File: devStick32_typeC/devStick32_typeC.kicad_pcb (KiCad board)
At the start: 2 copper layers, 35.6 x 82.6 mm, 9 parts, among them J1 Conn_01x06_Male, J2 Conn_01x14_Male, J3 Conn_01x14_Male, J4 Conn_02x05_Odd_Even, J5 CX70M-24P1

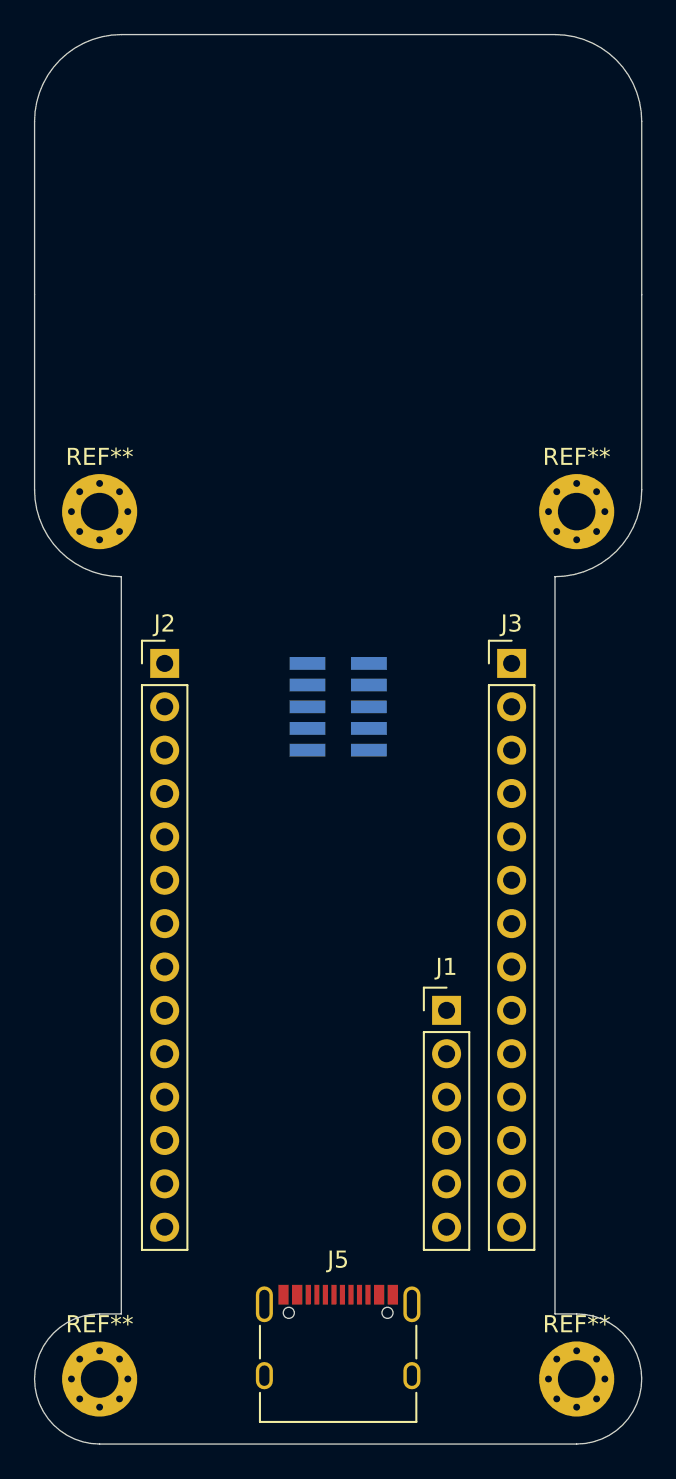
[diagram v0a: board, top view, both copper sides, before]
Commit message: Added ESP32-D0 on schema and PCB
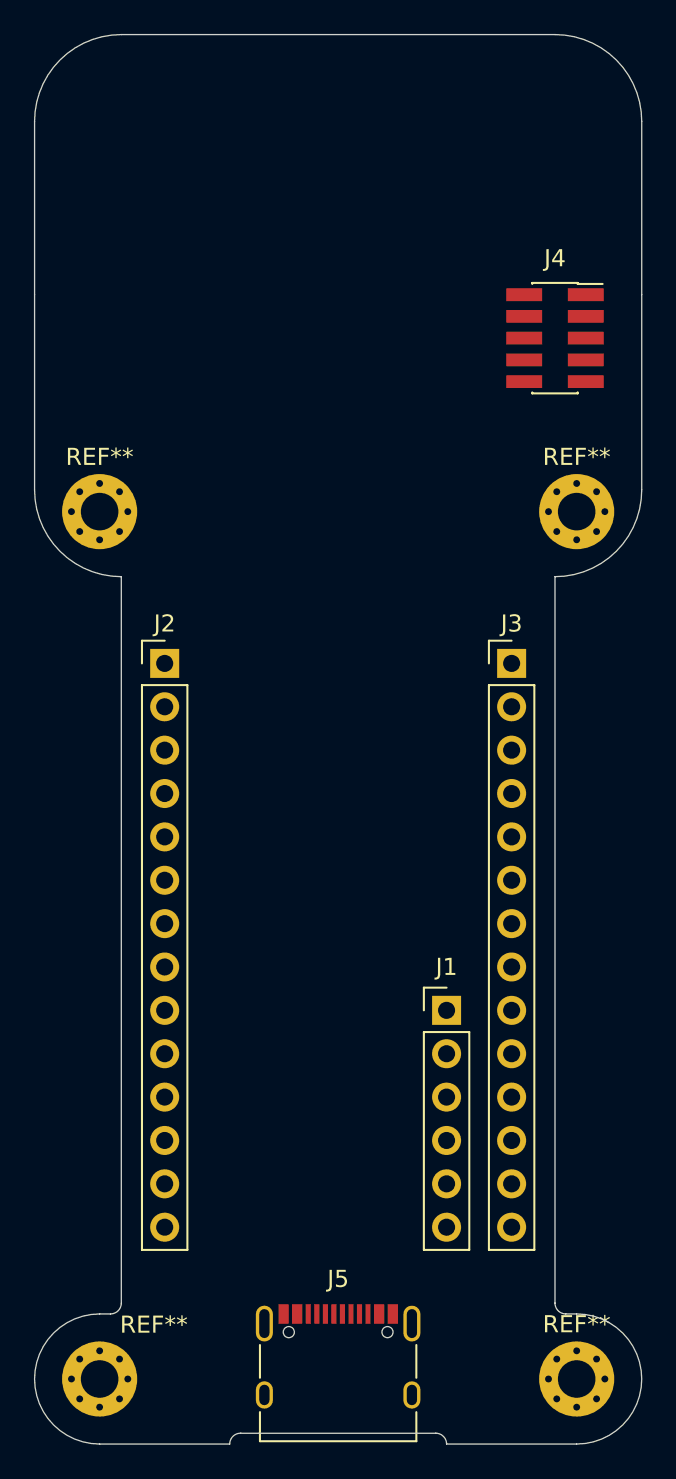
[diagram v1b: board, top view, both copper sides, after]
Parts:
- J4: moved to F.Cu
- moved J4 25.0 mm to (172.7, 64.8)
- moved J5 1.13 mm to (160.0, 125.6)
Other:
- outline, holes or cut-outs redrawn

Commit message: Added memory, xtal and labels
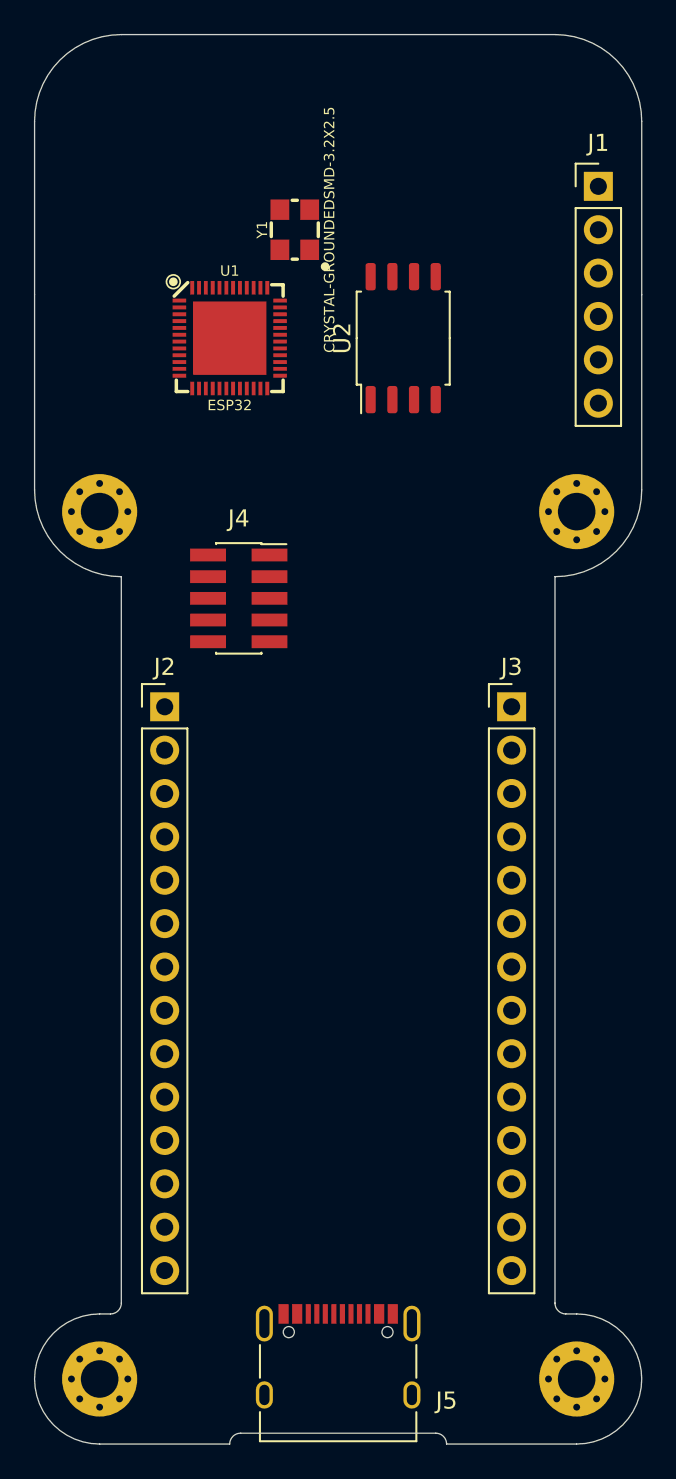
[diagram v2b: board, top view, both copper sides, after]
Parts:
- added U1: ESP32, Silicon-Standard:QFN48-0.4MM, F.Cu at (153.7, 64.8)
- added U2: W25Q32JVSS, Package_SO:SOIC-8_5.23x5.23mm_P1.27mm, F.Cu at (163.8, 64.8)
- added Y1: CRYSTAL-GROUNDEDSMD-3.2X2.5, CRYSTAL-SMD-3.2X2.5MM, F.Cu at (157.5, 58.4)
- moved J1 49.1 mm to (175.3, 55.9)
- moved J4 24.0 mm to (154.2, 80.0)
- moved J2 2.54 mm to (149.9, 86.4)
- moved J3 2.54 mm to (170.2, 86.4)
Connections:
- net Net-(J2-Pad10) renamed GPIO_8
- net Net-(J2-Pad11) renamed GPIO_9
- net Net-(J2-Pad12) renamed GPIO_10
- net Net-(J2-Pad13) renamed USB_PD_OUT
- net Net-(J2-Pad3) renamed GPIO_1
- net Net-(J2-Pad4) renamed GPIO_2
- net Net-(J2-Pad5) renamed GPIO_3
- net Net-(J2-Pad6) renamed GPIO_4
- net Net-(J2-Pad7) renamed GPIO_5
- net Net-(J2-Pad8) renamed GPIO_6
- net Net-(J2-Pad9) renamed GPIO_7
- net Net-(J3-Pad10) renamed GPIO_15
- net Net-(J3-Pad11) renamed GPIO_16
- net Net-(J3-Pad12) renamed GPIO_17
- net Net-(J3-Pad13) renamed VBUS
- net Net-(J3-Pad3) renamed GPIO_TX
- net Net-(J3-Pad4) renamed GPIO_RX
- net Net-(J3-Pad5) renamed RESET
- net Net-(J3-Pad6) renamed GPIO_11
- net Net-(J3-Pad7) renamed GPIO_12
- net Net-(J3-Pad8) renamed GPIO_13
- net Net-(J3-Pad9) renamed GPIO_14
- J2 pad 1: Net-(J2-Pad1) -> +3V3
- J2 pad 14: Net-(J2-Pad14) -> GND
- J2 pad 2: Net-(J2-Pad2) -> GND
- J3 pad 1: Net-(J3-Pad1) -> +3V3
- J3 pad 14: Net-(J3-Pad14) -> GND
- J3 pad 2: Net-(J3-Pad2) -> GND
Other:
- board text added: "3V3"
- board text added: "BOOT"
- board text added: "GND"
- board text added: "IO1"
- board text added: "IO10"
- board text added: "IO11"
- board text added: "IO12"
- board text added: "IO13"
- board text added: "IO14"
- board text added: "IO15"
- board text added: "IO16"
- board text added: "IO17"
- board text added: "IO2"
- board text added: "IO3"
- board text added: "IO4"
- board text added: "IO5"
- board text added: "IO6"
- board text added: "IO7"
- board text added: "IO8"
- board text added: "IO9"
- board text added: "RESET"
- board text added: "RX"
- board text added: "TX"
- board text added: "URX"
- board text added: "USB PD"
- board text added: "UTX"
- board text added: "VBUS"
- board text added: "VIN"
